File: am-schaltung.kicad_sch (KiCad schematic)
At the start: 71 parts, among them IC1 NE612, IC2 NE612, IC3 74HC74, IC4 TDA1072, IC5 74HCT4046, IC6 L78L05_SO8, IC7 L78L05_SO8, P1 50k, Q1 Q_NJFET_DGS, Q2 Q_NJFET_DGS, Q3 BC547, Q4 BC547, Q5 BC557

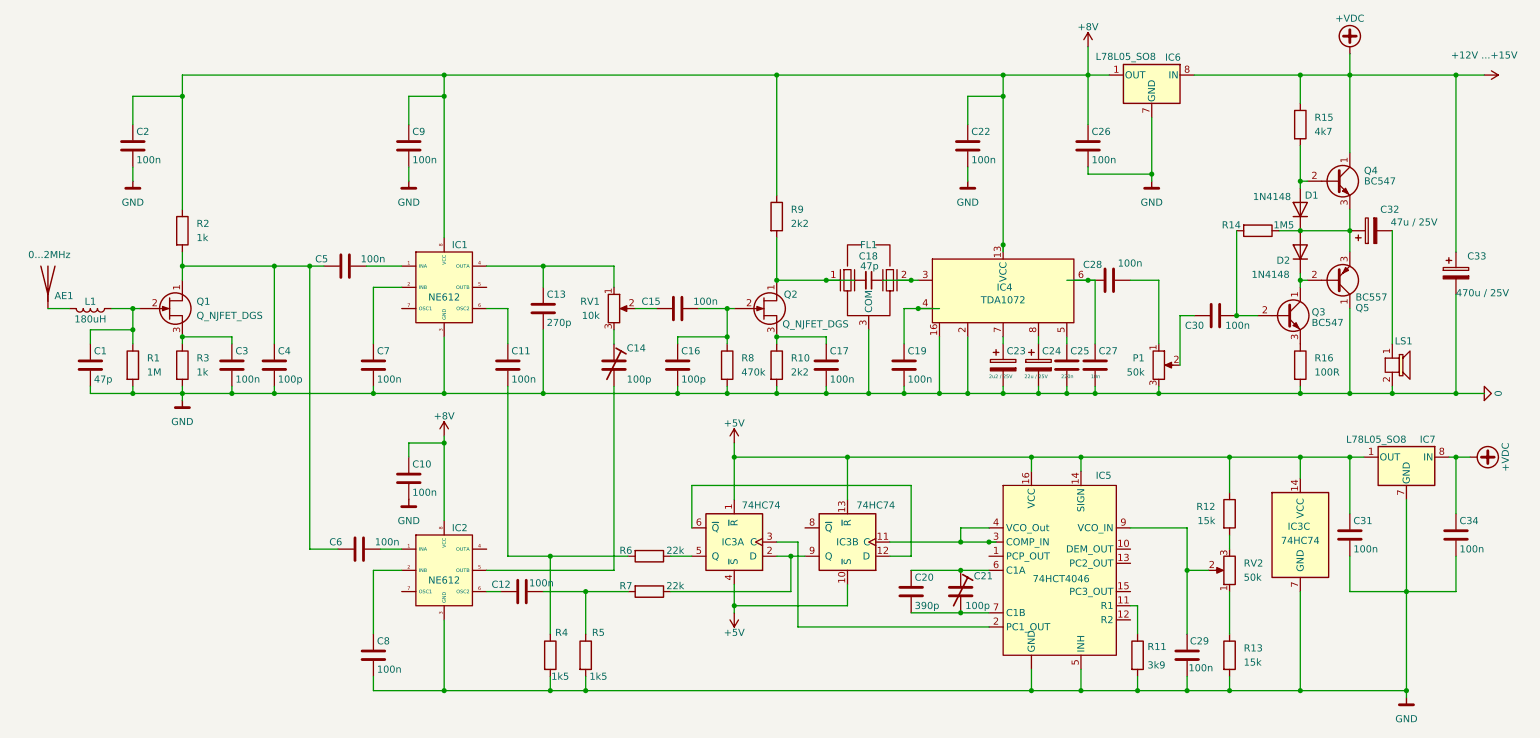
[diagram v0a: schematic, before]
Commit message: Updated AM Receiver Schematic with all Symbols. Footprint, manifest and data sheet still needed
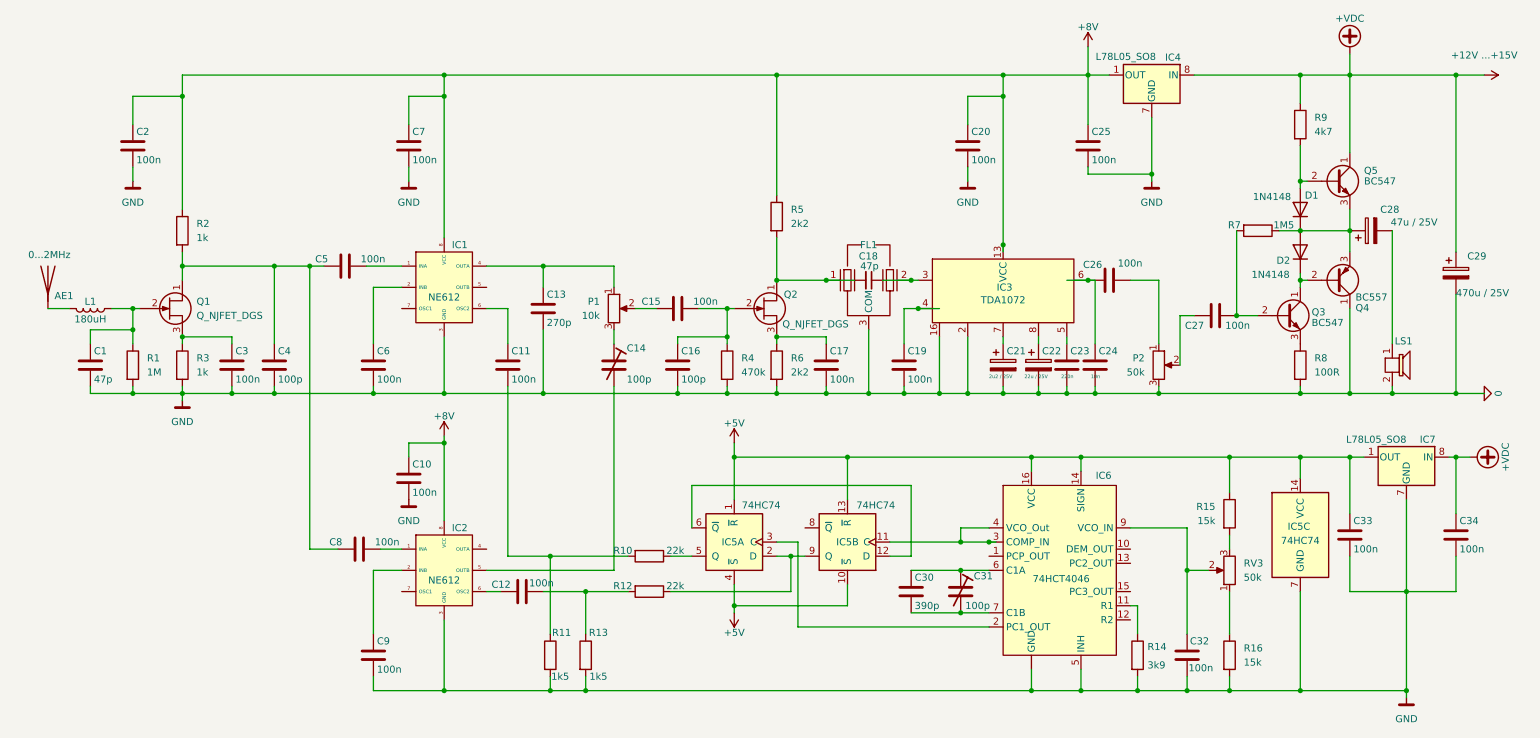
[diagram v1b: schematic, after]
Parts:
- renumbered C22 to C20, C23 to C21, C24 to C22, C25 to C23, C27 to C24, C26 to C25, C28 to C26, C30 to C27, C32 to C28, C33 to C29, C20 to C30, C21 to C31, C29 to C32, C31 to C33, C7 to C6, C9 to C7, C6 to C8, C8 to C9, IC4 to IC3, IC6 to IC4, IC3 to IC5, IC5 to IC6, RV1 to P1, P1 to P2, Q5 to Q4, Q4 to Q5, R6 to R10, R4 to R11, R7 to R12, R5 to R13, R11 to R14, R12 to R15, R13 to R16, R8 to R4, R9 to R5, R10 to R6, R14 to R7, R16 to R8, R15 to R9, RV2 to RV3
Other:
- company: HAWK -> (none)
- title: AM-Receiver -> (none)
